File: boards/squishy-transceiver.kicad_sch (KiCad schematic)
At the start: 99 parts, among them Q2 Q_PMOS_DGS, Q3 Q_DUAL_PMOS_S1G1D2S2G2D1, Q4 Q_DUAL_PMOS_S1G1D2S2G2D1, U1 THVD1452DGSR, U10 THVD1452DGSR, U11 FXL4TD245BQX, U13 THVD1452DGSR, U15 THVD1452DGSR, U16 FXL4TD245BQX, U17 THVD1452DGSR, U18 THVD1452DGSR, U2 FXL4TD245BQX, U20 FXL4TD245BQX, U21 THVD1452DGSR, U22 THVD1452DGSR, U23 FXL4TD245BQX, U24 THVD1452DGSR, U25 THVD1452DGSR, U27 FXL4TD245BQX, U28 THVD1452DGSR, U29 THVD1452DGSR, U30 FXL4TD245BQX, U31 THVD1452DGSR, U32 THVD1452DGSR, U33 FXL4TD245BQX, U34 THVD1452DGSR, U4 THVD1452DGSR, U6 THVD1452DGSR, U8 FXL4TD245BQX, U9 THVD1452DGSR

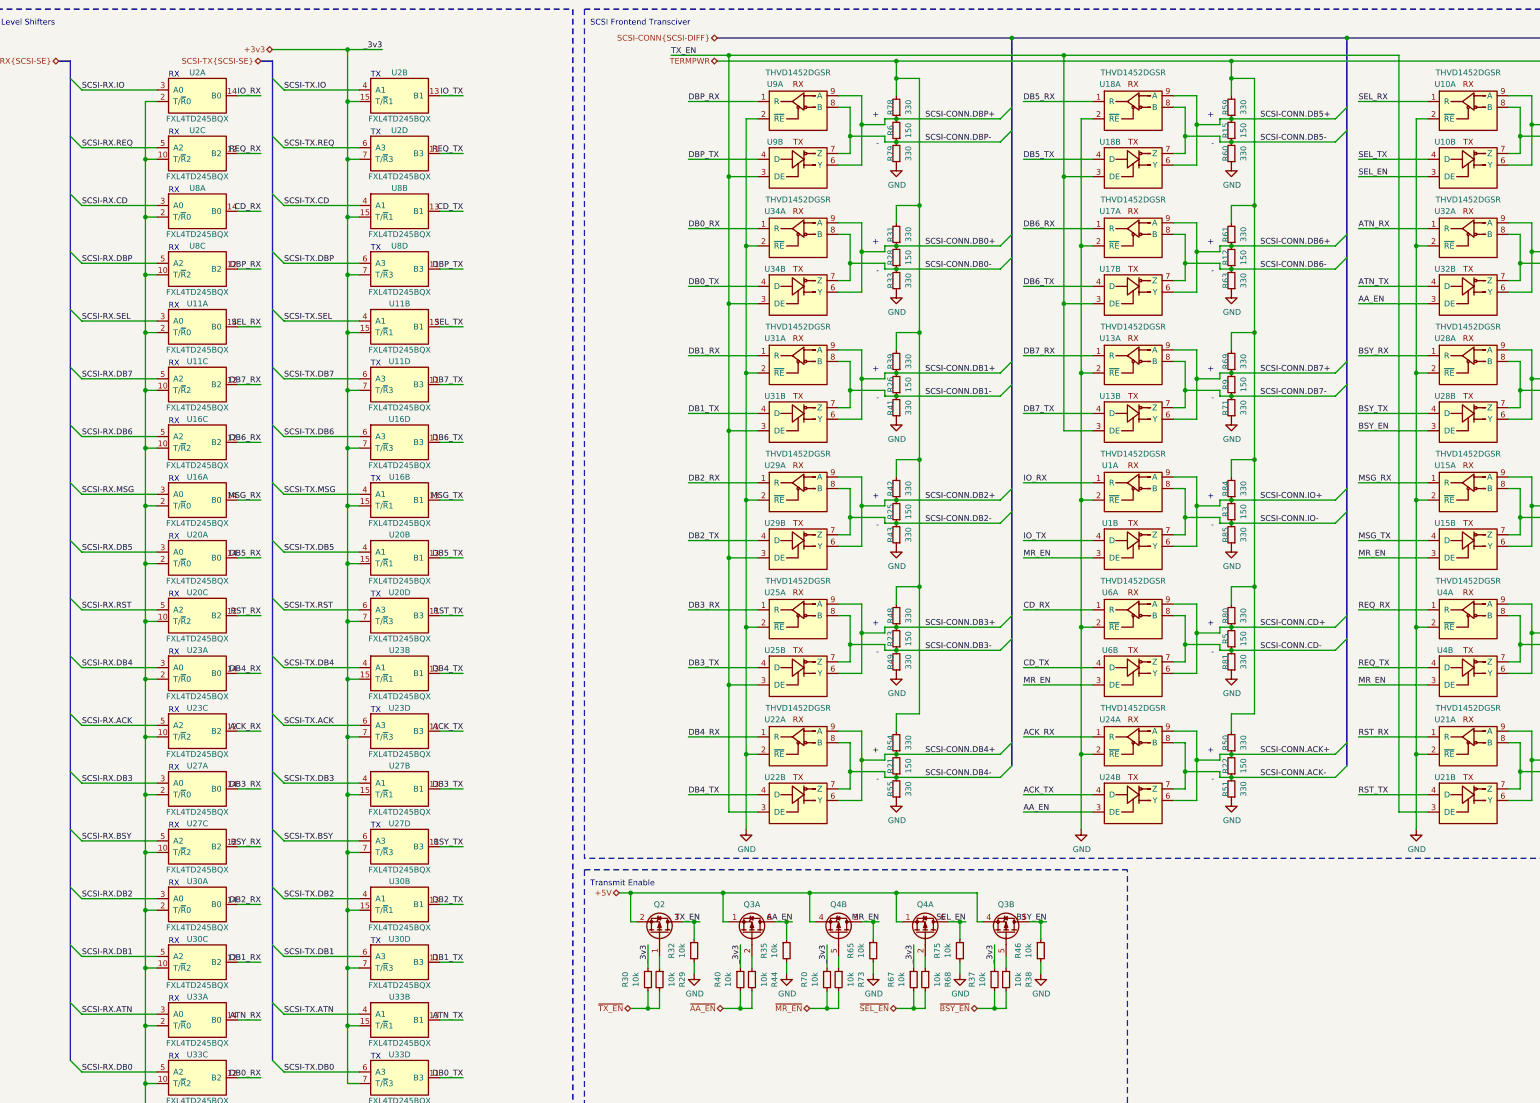
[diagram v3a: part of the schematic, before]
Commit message: hardware: supposedly fixed the pin ordering for all the scsi stuff, i hope
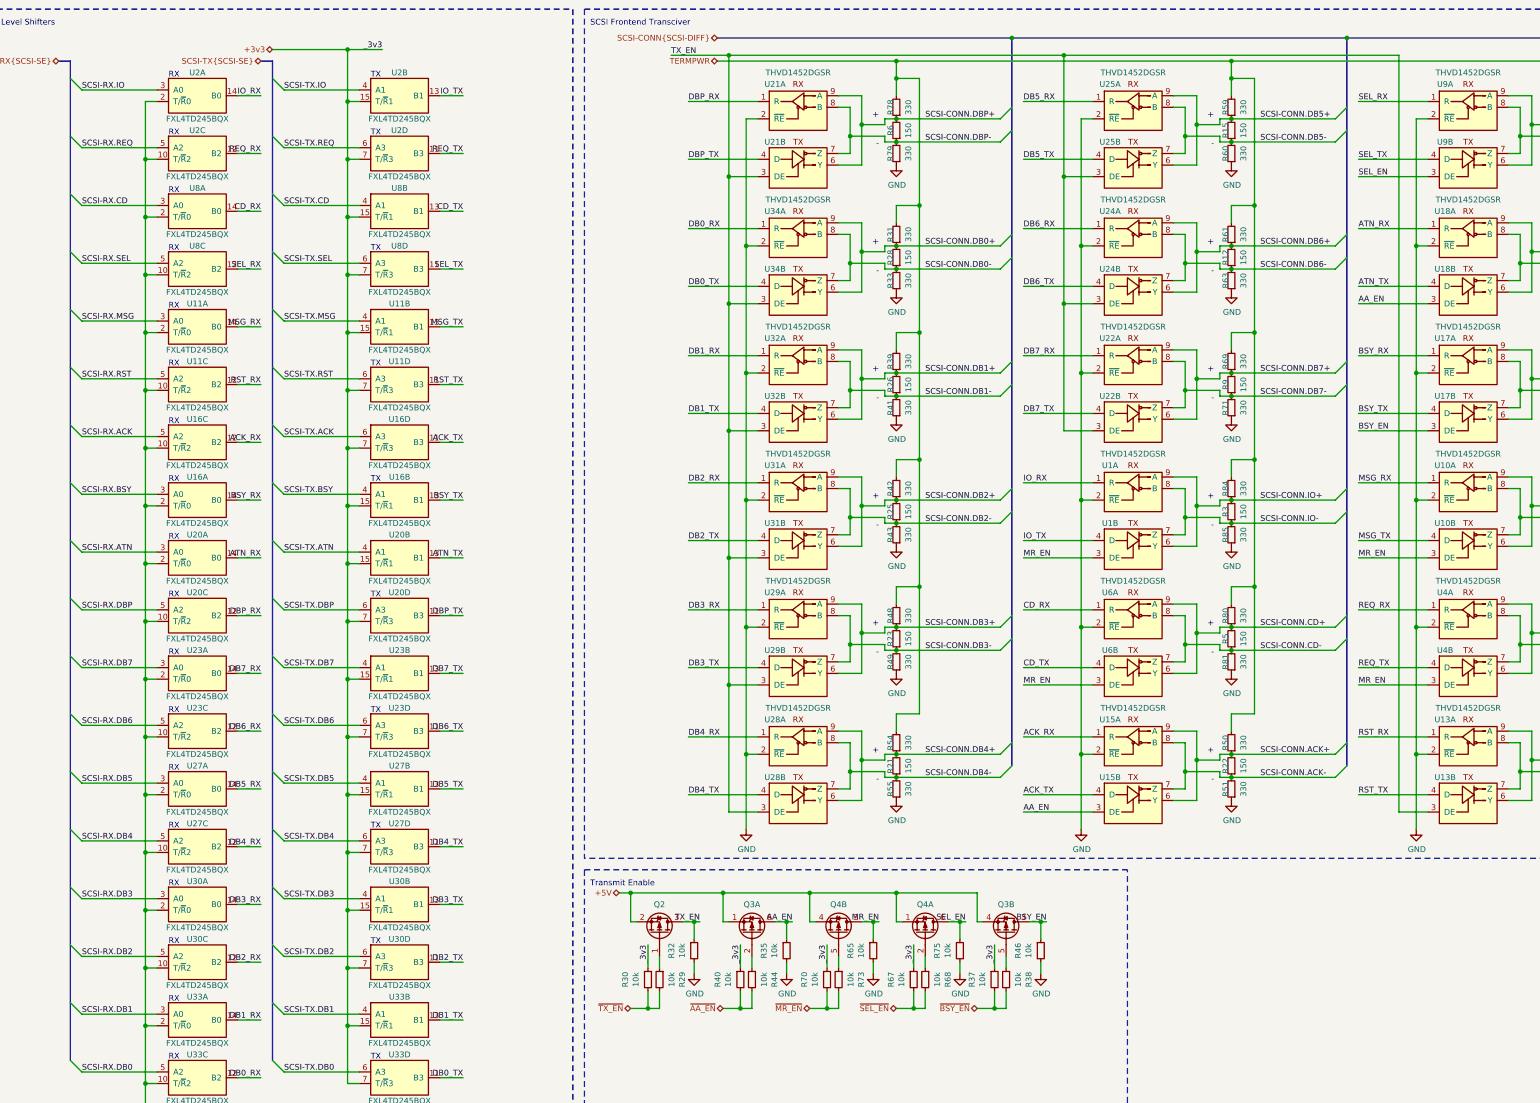
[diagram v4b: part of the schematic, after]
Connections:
- net AA_EN: now also U15.3 (DE), U18.3 (DE); no longer U24.3 (DE), U32.3 (DE)
- net ACK_RX: now also U15.1 (R), U16.12 (B2); no longer U23.12 (B2), U24.1 (R)
- net ACK_TX: now also U15.4 (D), U16.11 (B3); no longer U23.11 (B3), U24.4 (D)
- net ATN_RX: now also U18.1 (R), U20.14 (B0); no longer U32.1 (R), U33.14 (B0)
- net ATN_TX: now also U18.4 (D), U20.13 (B1); no longer U32.4 (D), U33.13 (B1)
- net BSY_EN: now also U17.3 (DE); no longer U28.3 (DE)
- net BSY_RX: now also U16.14 (B0), U17.1 (R); no longer U27.12 (B2), U28.1 (R)
- net BSY_TX: now also U16.13 (B1), U17.4 (D); no longer U27.11 (B3), U28.4 (D)
- net DB1_RX: now also U32.1 (R), U33.14 (B0); no longer U30.12 (B2), U31.1 (R)
- net DB1_TX: now also U32.4 (D), U33.13 (B1); no longer U30.11 (B3), U31.4 (D)
- net DB2_RX: now also U30.12 (B2), U31.1 (R); no longer U29.1 (R), U30.14 (B0)
- net DB2_TX: now also U30.11 (B3), U31.4 (D); no longer U29.4 (D), U30.13 (B1)
- net DB3_RX: now also U29.1 (R), U30.14 (B0); no longer U25.1 (R), U27.14 (B0)
- net DB3_TX: now also U29.4 (D), U30.13 (B1); no longer U25.4 (D), U27.13 (B1)
- net DB4_RX: now also U27.12 (B2), U28.1 (R); no longer U22.1 (R), U23.14 (B0)
- net DB4_TX: now also U27.11 (B3), U28.4 (D); no longer U22.4 (D), U23.13 (B1)
- net DB5_RX: now also U25.1 (R), U27.14 (B0); no longer U18.1 (R), U20.14 (B0)
- net DB5_TX: now also U25.4 (D), U27.13 (B1); no longer U18.4 (D), U20.13 (B1)
- net DB6_RX: now also U23.12 (B2), U24.1 (R); no longer U16.12 (B2), U17.1 (R)
- net DB6_TX: now also U23.11 (B3), U24.4 (D); no longer U16.11 (B3), U17.4 (D)
- net DB7_RX: now also U22.1 (R), U23.14 (B0); no longer U11.12 (B2), U13.1 (R)
- net DB7_TX: now also U22.4 (D), U23.13 (B1); no longer U11.11 (B3), U13.4 (D)
- net DBP_RX: now also U20.12 (B2), U21.1 (R); no longer U8.12 (B2), U9.1 (R)
- net DBP_TX: now also U20.11 (B3), U21.4 (D); no longer U8.11 (B3), U9.4 (D)
- net MR_EN: now also U10.3 (DE); no longer U15.3 (DE)
- net MSG_RX: now also U10.1 (R), U11.14 (B0); no longer U15.1 (R), U16.14 (B0)
- net MSG_TX: now also U10.4 (D), U11.13 (B1); no longer U15.4 (D), U16.13 (B1)
- net RST_RX: now also U11.12 (B2), U13.1 (R); no longer U20.12 (B2), U21.1 (R)
- net RST_TX: now also U11.11 (B3), U13.4 (D); no longer U20.11 (B3), U21.4 (D)
- net SCSI-CONN.ACK+: now also U15.6 (Y), U15.9 (A); no longer U24.6 (Y), U24.9 (A)
- net SCSI-CONN.ACK-: now also U15.7 (Z), U15.8 (B); no longer U24.7 (Z), U24.8 (B)
- net SCSI-CONN.ATN+: now also U18.6 (Y), U18.9 (A); no longer U32.6 (Y), U32.9 (A)
- net SCSI-CONN.ATN-: now also U18.7 (Z), U18.8 (B); no longer U32.7 (Z), U32.8 (B)
- net SCSI-CONN.BSY+: now also U17.6 (Y), U17.9 (A); no longer U28.6 (Y), U28.9 (A)
- net SCSI-CONN.BSY-: now also U17.7 (Z), U17.8 (B); no longer U28.7 (Z), U28.8 (B)
- net SCSI-CONN.DB1+: now also U32.6 (Y), U32.9 (A); no longer U31.6 (Y), U31.9 (A)
- net SCSI-CONN.DB1-: now also U32.7 (Z), U32.8 (B); no longer U31.7 (Z), U31.8 (B)
- net SCSI-CONN.DB2+: now also U31.6 (Y), U31.9 (A); no longer U29.6 (Y), U29.9 (A)
- net SCSI-CONN.DB2-: now also U31.7 (Z), U31.8 (B); no longer U29.7 (Z), U29.8 (B)
- net SCSI-CONN.DB3+: now also U29.6 (Y), U29.9 (A); no longer U25.6 (Y), U25.9 (A)
- net SCSI-CONN.DB3-: now also U29.7 (Z), U29.8 (B); no longer U25.7 (Z), U25.8 (B)
- net SCSI-CONN.DB4+: now also U28.6 (Y), U28.9 (A); no longer U22.6 (Y), U22.9 (A)
- net SCSI-CONN.DB4-: now also U28.7 (Z), U28.8 (B); no longer U22.7 (Z), U22.8 (B)
- net SCSI-CONN.DB5+: now also U25.6 (Y), U25.9 (A); no longer U18.6 (Y), U18.9 (A)
- net SCSI-CONN.DB5-: now also U25.7 (Z), U25.8 (B); no longer U18.7 (Z), U18.8 (B)
- net SCSI-CONN.DB6+: now also U24.6 (Y), U24.9 (A); no longer U17.6 (Y), U17.9 (A)
- net SCSI-CONN.DB6-: now also U24.7 (Z), U24.8 (B); no longer U17.7 (Z), U17.8 (B)
- net SCSI-CONN.DB7+: now also U22.6 (Y), U22.9 (A); no longer U13.6 (Y), U13.9 (A)
- net SCSI-CONN.DB7-: now also U22.7 (Z), U22.8 (B); no longer U13.7 (Z), U13.8 (B)
- net SCSI-CONN.DBP+: now also U21.6 (Y), U21.9 (A); no longer U9.6 (Y), U9.9 (A)
- net SCSI-CONN.DBP-: now also U21.7 (Z), U21.8 (B); no longer U9.7 (Z), U9.8 (B)
- net SCSI-CONN.MSG+: now also U10.6 (Y), U10.9 (A); no longer U15.6 (Y), U15.9 (A)
- net SCSI-CONN.MSG-: now also U10.7 (Z), U10.8 (B); no longer U15.7 (Z), U15.8 (B)
- net SCSI-CONN.RST+: now also U13.6 (Y), U13.9 (A); no longer U21.6 (Y), U21.9 (A)
- net SCSI-CONN.RST-: now also U13.7 (Z), U13.8 (B); no longer U21.7 (Z), U21.8 (B)
- net SCSI-CONN.SEL+: now also U9.6 (Y), U9.9 (A); no longer U10.6 (Y), U10.9 (A)
- net SCSI-CONN.SEL-: now also U9.7 (Z), U9.8 (B); no longer U10.7 (Z), U10.8 (B)
- net SCSI-RX.ACK: now also U16.5 (A2); no longer U23.5 (A2)
- net SCSI-RX.ATN: now also U20.3 (A0); no longer U33.3 (A0)
- net SCSI-RX.BSY: now also U16.3 (A0); no longer U27.5 (A2)
- net SCSI-RX.DB1: now also U33.3 (A0); no longer U30.5 (A2)
- net SCSI-RX.DB2: now also U30.5 (A2); no longer U30.3 (A0)
- net SCSI-RX.DB3: now also U30.3 (A0); no longer U27.3 (A0)
- net SCSI-RX.DB4: now also U27.5 (A2); no longer U23.3 (A0)
- net SCSI-RX.DB5: now also U27.3 (A0); no longer U20.3 (A0)
- net SCSI-RX.DB6: now also U23.5 (A2); no longer U16.5 (A2)
- net SCSI-RX.DB7: now also U23.3 (A0); no longer U11.5 (A2)
- net SCSI-RX.DBP: now also U20.5 (A2); no longer U8.5 (A2)
- net SCSI-RX.MSG: now also U11.3 (A0); no longer U16.3 (A0)
- net SCSI-RX.RST: now also U11.5 (A2); no longer U20.5 (A2)
- net SCSI-RX.SEL: now also U8.5 (A2); no longer U11.3 (A0)
- net SCSI-TX.ACK: now also U16.6 (A3); no longer U23.6 (A3)
- net SCSI-TX.ATN: now also U20.4 (A1); no longer U33.4 (A1)
- net SCSI-TX.BSY: now also U16.4 (A1); no longer U27.6 (A3)
- net SCSI-TX.DB1: now also U33.4 (A1); no longer U30.6 (A3)
- net SCSI-TX.DB2: now also U30.6 (A3); no longer U30.4 (A1)
- net SCSI-TX.DB3: now also U30.4 (A1); no longer U27.4 (A1)
- net SCSI-TX.DB4: now also U27.6 (A3); no longer U23.4 (A1)
- net SCSI-TX.DB5: now also U27.4 (A1); no longer U20.4 (A1)
- net SCSI-TX.DB6: now also U23.6 (A3); no longer U16.6 (A3)
- net SCSI-TX.DB7: now also U23.4 (A1); no longer U11.6 (A3)
- net SCSI-TX.DBP: now also U20.6 (A3); no longer U8.6 (A3)
- net SCSI-TX.MSG: now also U11.4 (A1); no longer U16.4 (A1)
- net SCSI-TX.RST: now also U11.6 (A3); no longer U20.6 (A3)
- net SCSI-TX.SEL: now also U8.6 (A3); no longer U11.4 (A1)
- net SEL_EN: now also U9.3 (DE); no longer U10.3 (DE)
- net SEL_RX: now also U8.12 (B2), U9.1 (R); no longer U10.1 (R), U11.14 (B0)
- net SEL_TX: now also U8.11 (B3), U9.4 (D); no longer U10.4 (D), U11.13 (B1)
- net TX_EN: now also U24.3 (DE), U28.3 (DE), U32.3 (DE); no longer U17.3 (DE), U18.3 (DE), U9.3 (DE)
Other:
- moved on the sheet: U10A, U10B, U13A, U13B, U15A, U15B, U17A, U17B, U18A, U18B, U21A, U21B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
